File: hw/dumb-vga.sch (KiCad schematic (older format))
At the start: 22 parts, among them IC1 74HC590N, IC2 74HC590N, IC3 74HC590N, IC4 74HC574N, P1 CONN_01X02, P2 CONN_01X03, P3 CONN_01X03, U1 A29040C, X1 VGAF

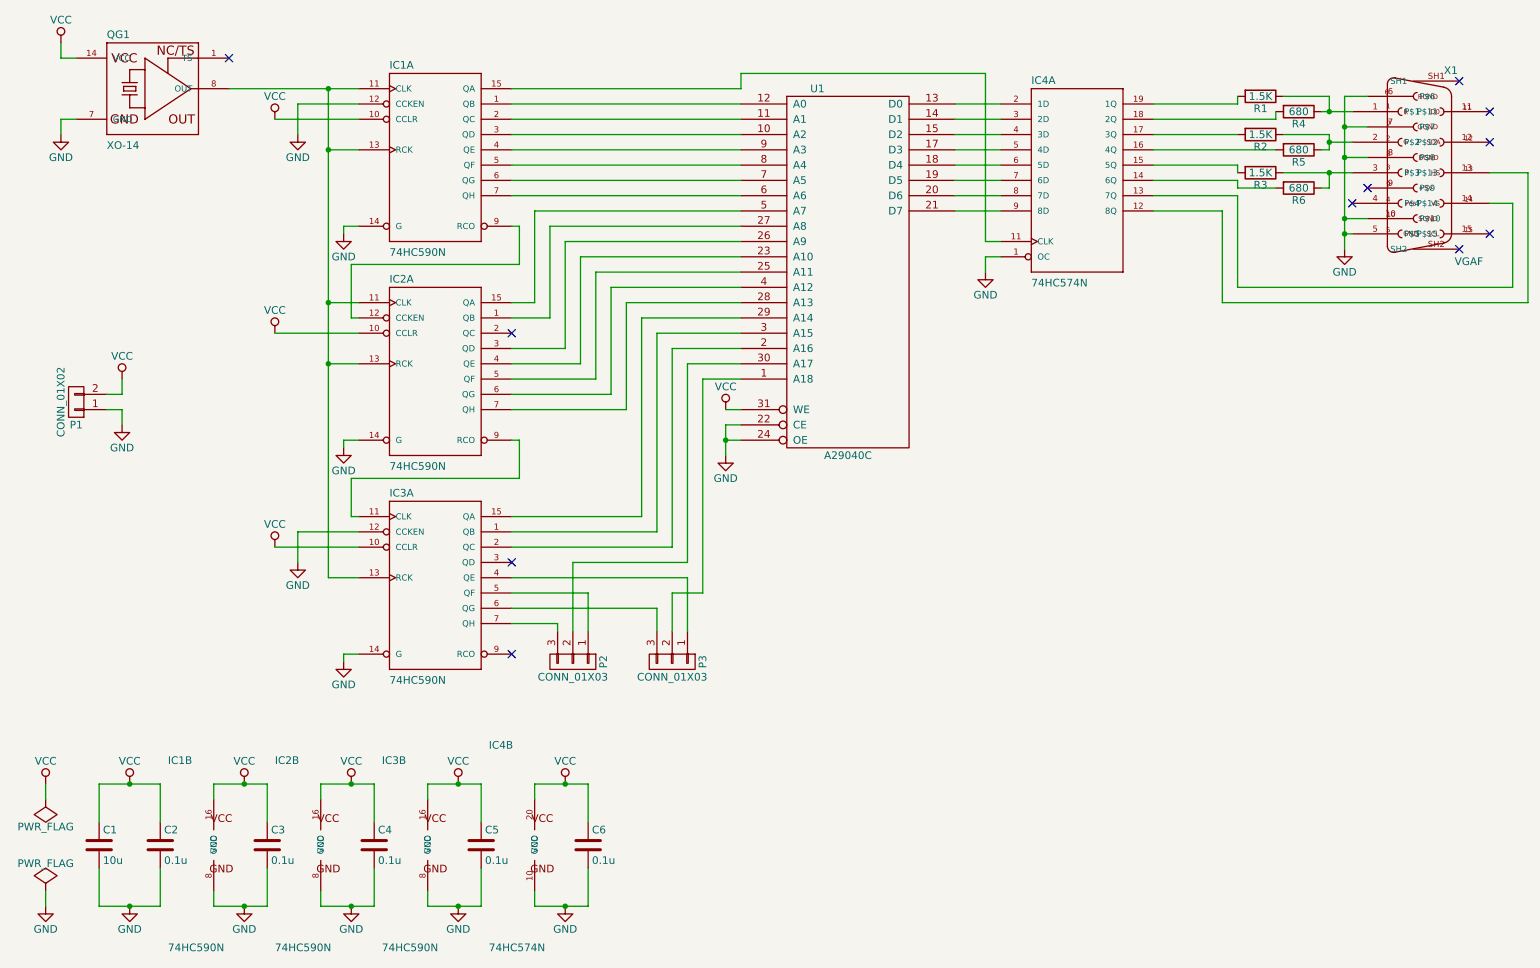
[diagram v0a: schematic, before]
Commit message: Rearranged memory lines to make PCB layout easier, laid out more PCB.
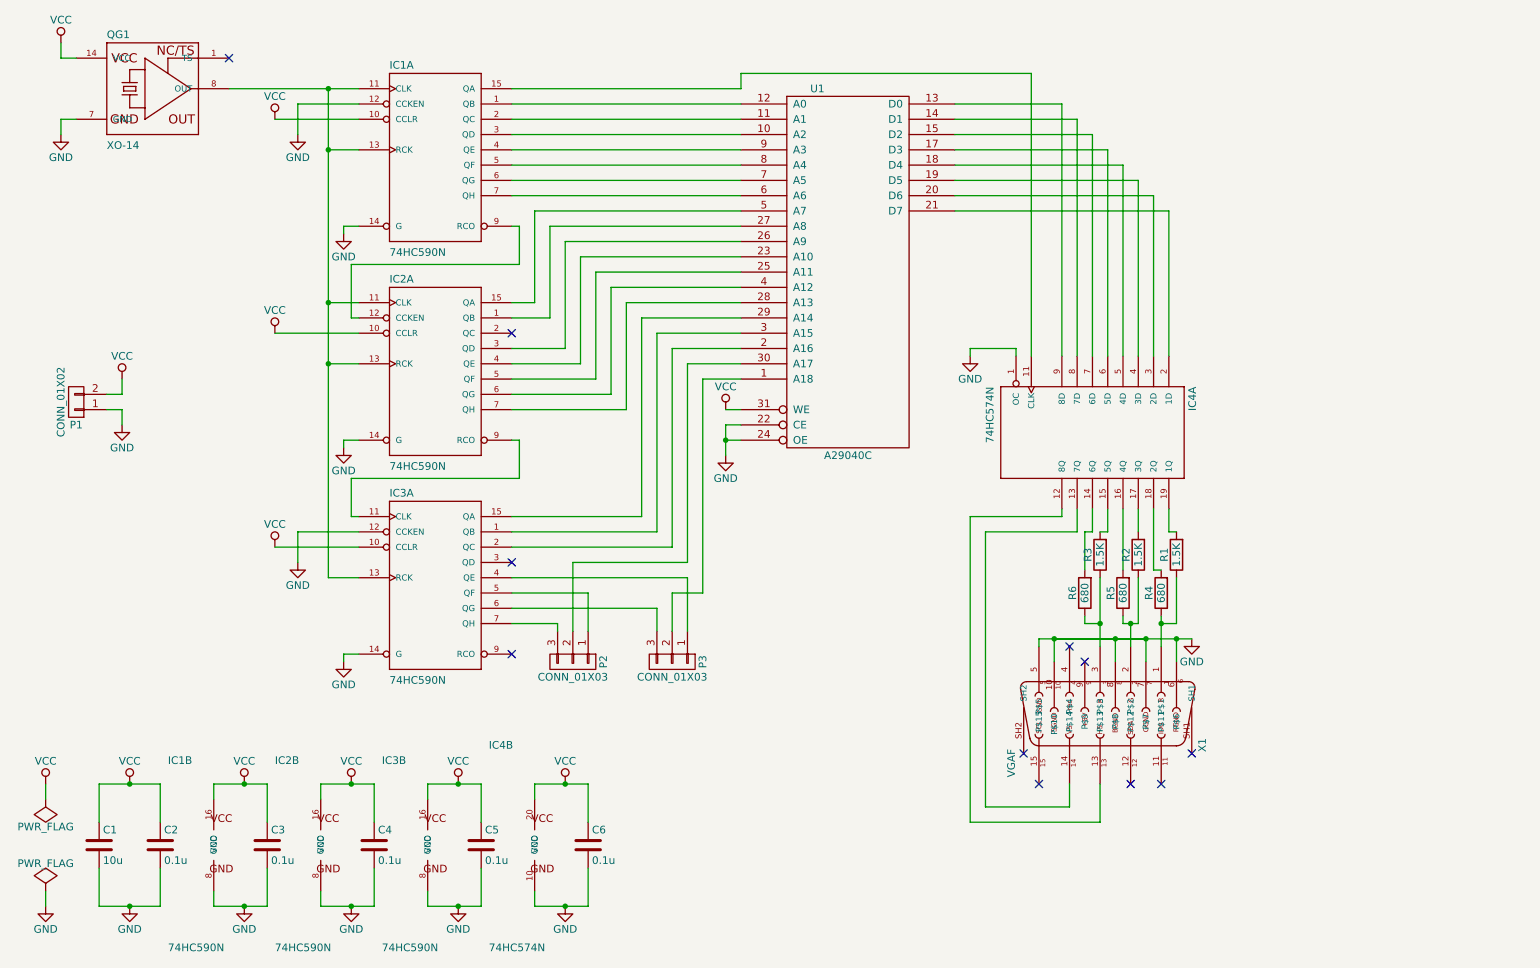
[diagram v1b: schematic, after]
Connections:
- net at U1.13 (D0): now also IC4.9 (8D); no longer IC4.2 (1D)
- net at U1.14 (D1): now also IC4.8 (7D); no longer IC4.3 (2D)
- net at U1.15 (D2): now also IC4.7 (6D); no longer IC4.4 (3D)
- net at U1.17 (D3): now also IC4.6 (5D); no longer IC4.5 (4D)
- net at U1.18 (D4): now also IC4.5 (4D); no longer IC4.6 (5D)
- net at U1.19 (D5): now also IC4.4 (3D); no longer IC4.7 (6D)
- net at U1.20 (D6): now also IC4.3 (2D); no longer IC4.8 (7D)
- net at U1.21 (D7): now also IC4.2 (1D); no longer IC4.9 (8D)
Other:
- moved on the sheet: IC4A, R1, R2, R3, R4, R5, R6, X1

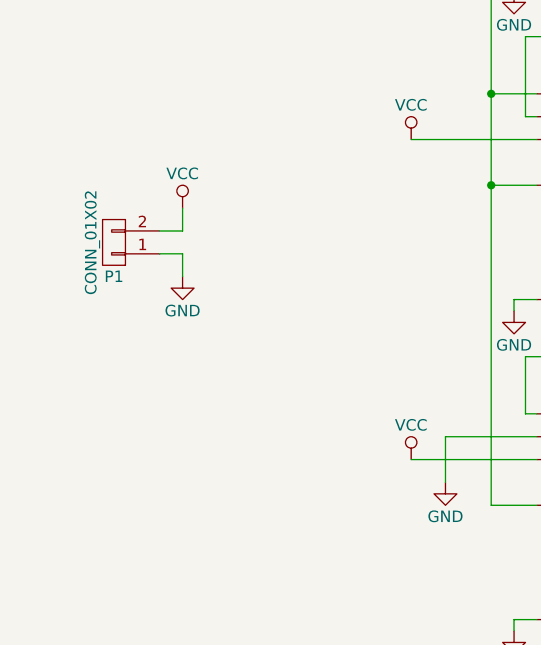
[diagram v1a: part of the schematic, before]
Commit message: Changed power connector for something I have
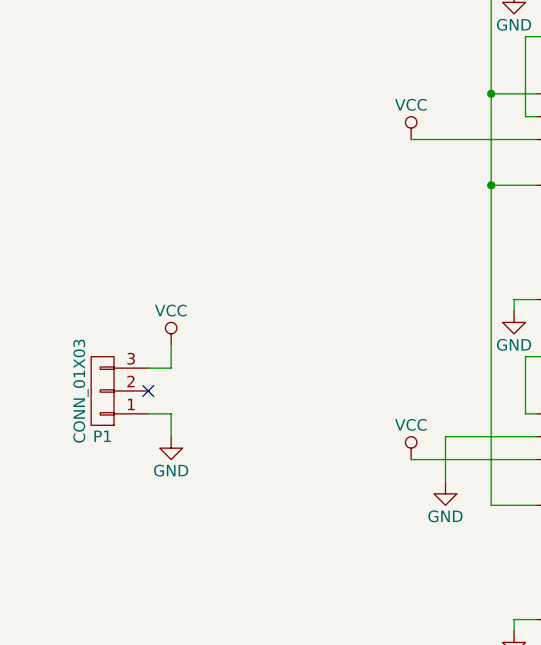
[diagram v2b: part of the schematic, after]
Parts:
- removed P1: CONN_01X02, Pin_Headers:Pin_Header_Angled_1x02, symbol CONN_01X02
- added P1: CONN_01X03, Pin_Headers:Pin_Header_Angled_1x03, symbol CONN_01X03
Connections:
- net GND: now also P1.1 (P1)
- net VCC: now also P1.3 (P3)
- no-connect marks 11 -> 12
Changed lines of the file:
@@
 $EndComp
 $Comp
-L VCC #PWR025
+L VCC #PWR024
 U 1 1 56DAD35F
 P 4250 5950
-F 0 "#PWR025" H 4250 5800 50  0001 C CNN
+F 0 "#PWR024" H 4250 5800 50  0001 C CNN
 F 1 "VCC" H 4250 6100 50  0000 C CNN
 F 2 "" H 4250 5950 50  0000 C CNN
@@
 $EndComp
 $Comp
-L GND #PWR026
+L GND #PWR025
 U 1 1 56DAD3AF
 P 4250 6750
-F 0 "#PWR026" H 4250 6500 50  0001 C CNN
+F 0 "#PWR025" H 4250 6500 50  0001 C CNN
 F 1 "GND" H 4250 6600 50  0000 C CNN
 F 2 "" H 4250 6750 50  0000 C CNN
@@
 NoConn ~ 2050 1200
 $Comp
-L VCC #PWR027
+L VCC #PWR026
 U 1 1 56E0A7F2
 P 950 1100
-F 0 "#PWR027" H 950 950 50  0001 C CNN
+F 0 "#PWR026" H 950 950 50  0001 C CNN
 F 1 "VCC" H 950 1250 50  0000 C CNN
 F 2 "" H 950 1100 50  0000 C CNN
@@
 $EndComp
 $Comp
-L GND #PWR028
+L GND #PWR027
 U 1 1 56E0A845
 P 950 1700
-F 0 "#PWR028" H 950 1450 50  0001 C CNN
+F 0 "#PWR027" H 950 1450 50  0001 C CNN
 F 1 "GND" H 950 1550 50  0000 C CNN
 F 2 "" H 950 1700 50  0000 C CNN
@@
 	950  1600 950  1700
 $Comp
-L CONN_01X02 P1
-U 1 1 56E0ABB2
-P 1050 3450
-F 0 "P1" H 1050 3600 50  0000 C CNN
-F 1 "CONN_01X02" V 1150 3450 50  0000 C CNN
-F 2 "Pin_Headers:Pin_Header_Angled_1x02" H 1050 3450 50  0001 C CNN
-F 3 "" H 1050 3450 50  0000 C CNN
-	1    1050 3450
-	-1   0    0    1
-$EndComp
-$Comp
-L VCC #PWR029
+L VCC #PWR028
 U 1 1 56E0AC4F
-P 1350 3300
-F 0 "#PWR029" H 1350 3150 50  0001 C CNN
-F 1 "VCC" H 1350 3450 50  0000 C CNN
-F 2 "" H 1350 3300 50  0000 C CNN
-F 3 "" H 1350 3300 50  0000 C CNN
-	1    1350 3300
-	1    0    0    -1
-$EndComp
-$Comp
-L GND #PWR030
+P 1300 3900
+F 0 "#PWR028" H 1300 3750 50  0001 C CNN
+F 1 "VCC" H 1300 4050 50  0000 C CNN
+F 2 "" H 1300 3900 50  0000 C CNN
+F 3 "" H 1300 3900 50  0000 C CNN
+	1    1300 3900
+	1    0    0    -1
+$EndComp
+$Comp
+L GND #PWR029
 U 1 1 56E0ACA5
-P 1350 3600
-F 0 "#PWR030" H 1350 3350 50  0001 C CNN
-F 1 "GND" H 1350 3450 50  0000 C CNN
-F 2 "" H 1350 3600 50  0000 C CNN
-F 3 "" H 1350 3600 50  0000 C CNN
-	1    1350 3600
-	1    0    0    -1
-$EndComp
-Wire Wire Line
-	1250 3400 1350 3400
-Wire Wire Line
-	1350 3400 1350 3300
-Wire Wire Line
-	1250 3500 1350 3500
-Wire Wire Line
-	1350 3500 1350 3600
+P 1300 4300
+F 0 "#PWR029" H 1300 4050 50  0001 C CNN
+F 1 "GND" H 1300 4150 50  0000 C CNN
+F 2 "" H 1300 4300 50  0000 C CNN
+F 3 "" H 1300 4300 50  0000 C CNN
+	1    1300 4300
+	1    0    0    -1
+$EndComp
+Wire Wire Line
+	1200 4200 1300 4200
+Wire Wire Line
+	1300 4200 1300 4300
 $Comp
 L CONN_01X03 P3
@@
 Connection ~ 8250 5000
 $Comp
-L GND #PWR?
+L GND #PWR030
 U 1 1 56E9DC88
 P 6900 3150
-F 0 "#PWR?" H 6900 2900 50  0001 C CNN
+F 0 "#PWR030" H 6900 2900 50  0001 C CNN
 F 1 "GND" H 6900 3000 50  0000 C CNN
 F 2 "" H 6900 3150 50  0000 C CNN
@@
 Wire Wire Line
 	7500 1500 6800 1500
+$Comp
+L CONN_01X03 P1
+U 1 1 56E9ECEC
+P 1000 4100
+F 0 "P1" H 1000 4300 50  0000 C CNN
+F 1 "CONN_01X03" V 1100 4100 50  0000 C CNN
+F 2 "Pin_Headers:Pin_Header_Angled_1x03" H 1000 4100 50  0001 C CNN
+F 3 "" H 1000 4100 50  0000 C CNN
+	1    1000 4100
+	-1   0    0    1
+$EndComp
+Wire Wire Line
+	1200 4000 1300 4000
+Wire Wire Line
+	1300 4000 1300 3900
+NoConn ~ 1200 4100
 $EndSCHEMATC

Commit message: Switched to VGA connector with soldermask on the bottom
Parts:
- X1: footprint HD15_B:HD15_B-HD15F -> hw:hd15f
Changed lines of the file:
@@
 F 0 "X1" H 8050 5990 50  0000 L BNN
 F 1 "VGAF" H 8120 4740 50  0000 L BNN
-F 2 "HD15_B:HD15_B-HD15F" H 7850 5600 50  0001 C CNN
+F 2 "hw:hd15f" H 7850 5600 50  0001 C CNN
 F 3 "" H 7850 5450 60  0000 C CNN
 	1    7850 5450

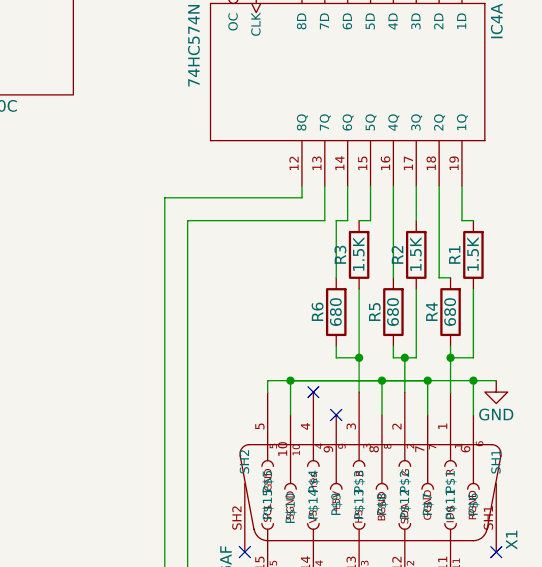
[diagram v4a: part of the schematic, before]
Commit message: Switch resistors around to make programming easier
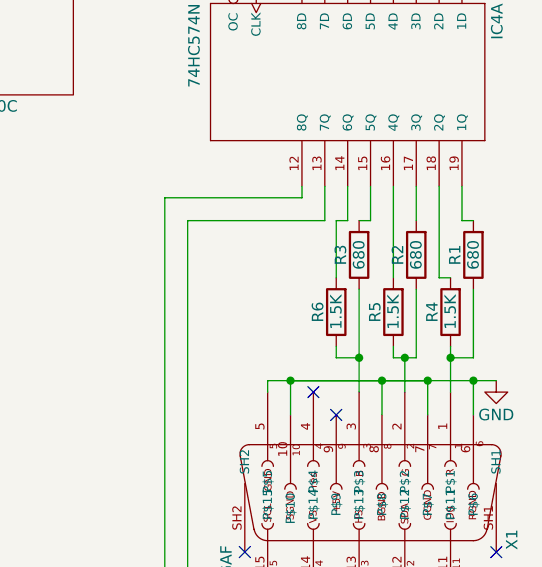
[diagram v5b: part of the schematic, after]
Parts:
- R1, R2, R3: value 1.5K -> 680
- R4, R5, R6: value 680 -> 1.5K
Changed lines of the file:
@@
 P 8150 4700
 F 0 "R4" V 8230 4700 50  0000 C CNN
-F 1 "680" V 8150 4700 50  0000 C CNN
+F 1 "1.5K" V 8150 4700 50  0000 C CNN
 F 2 "Resistors_ThroughHole:Resistor_Horizontal_RM10mm" V 8080 4700 50  0001 C CNN
 F 3 "" H 8150 4700 50  0000 C CNN
@@
 P 7900 4700
 F 0 "R5" V 7980 4700 50  0000 C CNN
-F 1 "680" V 7900 4700 50  0000 C CNN
+F 1 "1.5K" V 7900 4700 50  0000 C CNN
 F 2 "Resistors_ThroughHole:Resistor_Horizontal_RM10mm" V 7830 4700 50  0001 C CNN
 F 3 "" H 7900 4700 50  0000 C CNN
@@
 P 7650 4700
 F 0 "R6" V 7730 4700 50  0000 C CNN
-F 1 "680" V 7650 4700 50  0000 C CNN
+F 1 "1.5K" V 7650 4700 50  0000 C CNN
 F 2 "Resistors_ThroughHole:Resistor_Horizontal_RM10mm" V 7580 4700 50  0001 C CNN
 F 3 "" H 7650 4700 50  0000 C CNN
@@
 P 8250 4450
 F 0 "R1" V 8330 4450 50  0000 C CNN
-F 1 "1.5K" V 8250 4450 50  0000 C CNN
+F 1 "680" V 8250 4450 50  0000 C CNN
 F 2 "Resistors_ThroughHole:Resistor_Horizontal_RM10mm" V 8180 4450 50  0001 C CNN
 F 3 "" H 8250 4450 50  0000 C CNN
@@
 P 8000 4450
 F 0 "R2" V 8080 4450 50  0000 C CNN
-F 1 "1.5K" V 8000 4450 50  0000 C CNN
+F 1 "680" V 8000 4450 50  0000 C CNN
 F 2 "Resistors_ThroughHole:Resistor_Horizontal_RM10mm" V 7930 4450 50  0001 C CNN
 F 3 "" H 8000 4450 50  0000 C CNN
@@
 P 7750 4450
 F 0 "R3" V 7830 4450 50  0000 C CNN
-F 1 "1.5K" V 7750 4450 50  0000 C CNN
+F 1 "680" V 7750 4450 50  0000 C CNN
 F 2 "Resistors_ThroughHole:Resistor_Horizontal_RM10mm" V 7680 4450 50  0001 C CNN
 F 3 "" H 7750 4450 50  0000 C CNN
